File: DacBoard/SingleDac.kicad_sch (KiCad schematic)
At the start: 3 parts, among them U5 AD5725

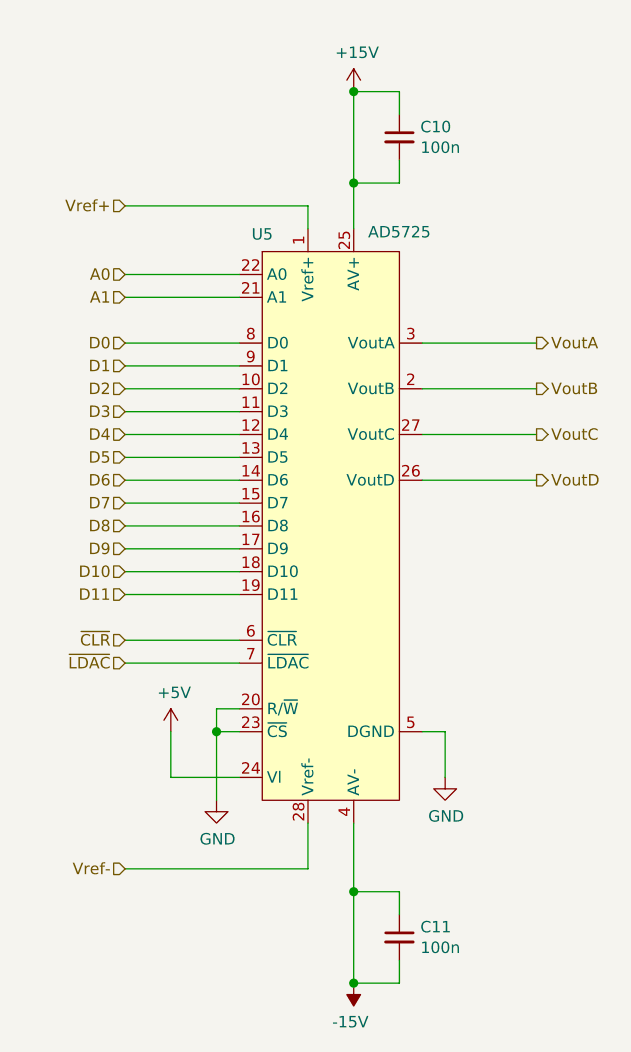
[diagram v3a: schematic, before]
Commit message: Schematic finalized (for now); Begin PCB
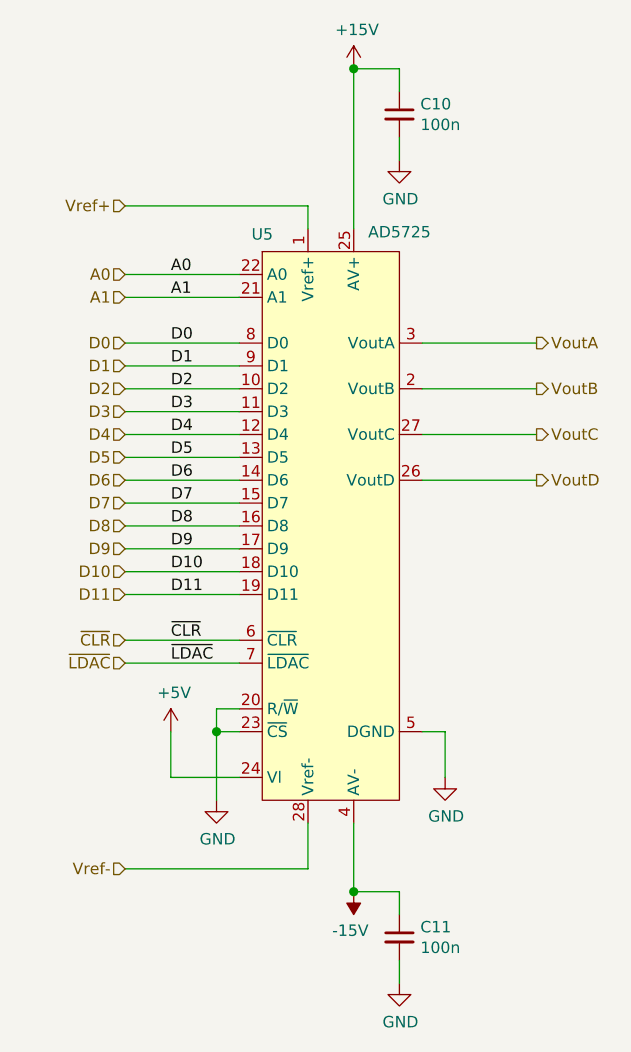
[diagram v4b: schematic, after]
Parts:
- C10, C11: footprint (none) -> Capacitor_SMD:C_0805_2012Metric_Pad1.18x1.45mm_HandSolder
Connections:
- net +15V: no longer C10.2
- net -15V: no longer C11.2
- net GND: now also C10.2, C11.2
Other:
- moved on the sheet: C10
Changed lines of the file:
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@@
   (paper "A4")
   (junction (at 167.64 104.14) (diameter 1.016) (color 0 0 0 0))
-  (junction (at 182.88 33.02) (diameter 1.016) (color 0 0 0 0))
-  (junction (at 182.88 43.18) (diameter 1.016) (color 0 0 0 0))
+  (junction (at 182.88 30.48) (diameter 1.016) (color 0 0 0 0))
   (junction (at 182.88 121.92) (diameter 1.016) (color 0 0 0 0))
-  (junction (at 182.88 132.08) (diameter 1.016) (color 0 0 0 0))
   (wire (pts (xy 157.48 45.72) (xy 177.8 45.72))
     (stroke (width 0) (type solid) (color 0 0 0 0))
@@
     (stroke (width 0) (type solid) (color 0 0 0 0))
   )
-  (wire (pts (xy 182.88 33.02) (xy 182.88 43.18))
-    (stroke (width 0) (type solid) (color 0 0 0 0))
-  )
-  (wire (pts (xy 182.88 33.02) (xy 187.96 33.02))
-    (stroke (width 0) (type solid) (color 0 0 0 0))
-  )
-  (wire (pts (xy 182.88 43.18) (xy 182.88 48.26))
-    (stroke (width 0) (type solid) (color 0 0 0 0))
-  )
-  (wire (pts (xy 182.88 43.18) (xy 187.96 43.18))
+  (wire (pts (xy 182.88 30.48) (xy 182.88 48.26))
+    (stroke (width 0) (type solid) (color 0 0 0 0))
+  )
+  (wire (pts (xy 182.88 30.48) (xy 187.96 30.48))
     (stroke (width 0) (type solid) (color 0 0 0 0))
   )
@@
     (stroke (width 0) (type solid) (color 0 0 0 0))
   )
-  (wire (pts (xy 182.88 132.08) (xy 182.88 121.92))
-    (stroke (width 0) (type solid) (color 0 0 0 0))
-  )
-  (wire (pts (xy 182.88 132.08) (xy 187.96 132.08))
-    (stroke (width 0) (type solid) (color 0 0 0 0))
-  )
-  (wire (pts (xy 187.96 33.02) (xy 187.96 35.56))
-    (stroke (width 0) (type solid) (color 0 0 0 0))
-  )
-  (wire (pts (xy 187.96 43.18) (xy 187.96 40.64))
+  (wire (pts (xy 187.96 30.48) (xy 187.96 33.02))
+    (stroke (width 0) (type solid) (color 0 0 0 0))
+  )
+  (wire (pts (xy 187.96 40.64) (xy 187.96 38.1))
     (stroke (width 0) (type solid) (color 0 0 0 0))
   )
@@
   (wire (pts (xy 193.04 104.14) (xy 193.04 109.22))
     (stroke (width 0) (type solid) (color 0 0 0 0))
+  )
+  (label "A0" (at 162.56 53.34 0)
+    (effects (font (size 1.27 1.27)) (justify left bottom))
+  )
+  (label "A1" (at 162.56 55.88 0)
+    (effects (font (size 1.27 1.27)) (justify left bottom))
+  )
+  (label "D0" (at 162.56 60.96 0)
+    (effects (font (size 1.27 1.27)) (justify left bottom))
+  )
+  (label "D1" (at 162.56 63.5 0)
+    (effects (font (size 1.27 1.27)) (justify left bottom))
+  )
+  (label "D2" (at 162.56 66.04 0)
+    (effects (font (size 1.27 1.27)) (justify left bottom))
+  )
+  (label "D3" (at 162.56 68.58 0)
+    (effects (font (size 1.27 1.27)) (justify left bottom))
+  )
+  (label "D4" (at 162.56 71.12 0)
+    (effects (font (size 1.27 1.27)) (justify left bottom))
+  )
+  (label "D5" (at 162.56 73.66 0)
+    (effects (font (size 1.27 1.27)) (justify left bottom))
+  )
+  (label "D6" (at 162.56 76.2 0)
+    (effects (font (size 1.27 1.27)) (justify left bottom))
+  )
+  (label "D7" (at 162.56 78.74 0)
+    (effects (font (size 1.27 1.27)) (justify left bottom))
+  )
+  (label "D8" (at 162.56 81.28 0)
+    (effects (font (size 1.27 1.27)) (justify left bottom))
+  )
+  (label "D9" (at 162.56 83.82 0)
+    (effects (font (size 1.27 1.27)) (justify left bottom))
+  )
+  (label "D10" (at 162.56 86.36 0)
+    (effects (font (size 1.27 1.27)) (justify left bottom))
+  )
+  (label "D11" (at 162.56 88.9 0)
+    (effects (font (size 1.27 1.27)) (justify left bottom))
+  )
+  (label "~CLR" (at 162.56 93.98 0)
+    (effects (font (size 1.27 1.27)) (justify left bottom))
+  )
+  (label "~LDAC" (at 162.56 96.52 0)
+    (effects (font (size 1.27 1.27)) (justify left bottom))
   )
   (hierarchical_label "Vref+" (shape input) (at 157.48 45.72 180)
@@
     (pin "1")
   )
-  (symbol (lib_id "power:+15V") (at 182.88 33.02 0)
-    (in_bom yes) (on_board yes)
-    (property "Reference" "#PWR0128" (id 0) (at 182.88 36.83 0)
-      (effects (font (size 1.27 1.27)) hide)
-    )
-    (property "Value" "+15V" (id 1) (at 183.2483 28.6956 0))
-    (property "Footprint" "" (id 2) (at 182.88 33.02 0)
-      (effects (font (size 1.27 1.27)) hide)
-    )
-    (property "Datasheet" "" (id 3) (at 182.88 33.02 0)
-      (effects (font (size 1.27 1.27)) hide)
-    )
-    (pin "1")
-  )
-  (symbol (lib_id "power:-15V") (at 182.88 132.08 180)
-    (in_bom yes) (on_board yes)
-    (property "Reference" "#PWR0131" (id 0) (at 182.88 134.62 0)
-      (effects (font (size 1.27 1.27)) hide)
-    )
-    (property "Value" "-15V" (id 1) (at 182.5117 136.4044 0))
-    (property "Footprint" "" (id 2) (at 182.88 132.08 0)
-      (effects (font (size 1.27 1.27)) hide)
-    )
-    (property "Datasheet" "" (id 3) (at 182.88 132.08 0)
+  (symbol (lib_id "power:+15V") (at 182.88 30.48 0)
+    (in_bom yes) (on_board yes)
+    (property "Reference" "#PWR0128" (id 0) (at 182.88 34.29 0)
+      (effects (font (size 1.27 1.27)) hide)
+    )
+    (property "Value" "+15V" (id 1) (at 183.2483 26.1556 0))
+    (property "Footprint" "" (id 2) (at 182.88 30.48 0)
+      (effects (font (size 1.27 1.27)) hide)
+    )
+    (property "Datasheet" "" (id 3) (at 182.88 30.48 0)
+      (effects (font (size 1.27 1.27)) hide)
+    )
+    (pin "1")
+  )
+  (symbol (lib_id "power:-15V") (at 182.88 121.92 180)
+    (in_bom yes) (on_board yes)
+    (property "Reference" "#PWR0131" (id 0) (at 182.88 124.46 0)
+      (effects (font (size 1.27 1.27)) hide)
+    )
+    (property "Value" "-15V" (id 1) (at 182.5117 126.2444 0))
+    (property "Footprint" "" (id 2) (at 182.88 121.92 0)
+      (effects (font (size 1.27 1.27)) hide)
+    )
+    (property "Datasheet" "" (id 3) (at 182.88 121.92 0)
       (effects (font (size 1.27 1.27)) hide)
     )
@@
     (pin "1")
   )
+  (symbol (lib_id "power:GND") (at 187.96 40.64 0)
+    (in_bom yes) (on_board yes)
+    (property "Reference" "#PWR012" (id 0) (at 187.96 46.99 0)
+      (effects (font (size 1.27 1.27)) hide)
+    )
+    (property "Value" "GND" (id 1) (at 188.0743 44.9644 0))
+    (property "Footprint" "" (id 2) (at 187.96 40.64 0)
+      (effects (font (size 1.27 1.27)) hide)
+    )
+    (property "Datasheet" "" (id 3) (at 187.96 40.64 0)
+      (effects (font (size 1.27 1.27)) hide)
+    )
+    (pin "1")
+  )
+  (symbol (lib_id "power:GND") (at 187.96 132.08 0)
+    (in_bom yes) (on_board yes)
+    (property "Reference" "#PWR013" (id 0) (at 187.96 138.43 0)
+      (effects (font (size 1.27 1.27)) hide)
+    )
+    (property "Value" "GND" (id 1) (at 188.0743 136.4044 0))
+    (property "Footprint" "" (id 2) (at 187.96 132.08 0)
+      (effects (font (size 1.27 1.27)) hide)
+    )
+    (property "Datasheet" "" (id 3) (at 187.96 132.08 0)
+      (effects (font (size 1.27 1.27)) hide)
+    )
+    (pin "1")
+  )
   (symbol (lib_id "power:GND") (at 193.04 109.22 0)
     (in_bom yes) (on_board yes)
@@
     (pin "1")
   )
-  (symbol (lib_id "Device:C_Small") (at 187.96 38.1 0)
-    (in_bom yes) (on_board yes)
-    (property "Reference" "C10" (id 0) (at 190.2842 36.9506 0)
+  (symbol (lib_id "Device:C_Small") (at 187.96 35.56 0)
+    (in_bom yes) (on_board yes)
+    (property "Reference" "C10" (id 0) (at 190.2842 34.4106 0)
       (effects (font (size 1.27 1.27)) (justify left))
     )
-    (property "Value" "100n" (id 1) (at 190.2968 39.243 0)
+    (property "Value" "100n" (id 1) (at 190.2968 36.703 0)
       (effects (font (size 1.27 1.27)) (justify left))
     )
-    (property "Footprint" "" (id 2) (at 187.96 38.1 0)
-      (effects (font (size 1.27 1.27)) hide)
-    )
-    (property "Datasheet" "~" (id 3) (at 187.96 38.1 0)
+    (property "Footprint" "Capacitor_SMD:C_0805_2012Metric_Pad1.18x1.45mm_HandSolder" (id 2) (at 187.96 35.56 0)
+      (effects (font (size 1.27 1.27)) hide)
+    )
+    (property "Datasheet" "~" (id 3) (at 187.96 35.56 0)
       (effects (font (size 1.27 1.27)) hide)
     )
@@
       (effects (font (size 1.27 1.27)) (justify left))
     )
-    (property "Footprint" "" (id 2) (at 187.96 127 0)
-      (effects (font (size 1.27 1.27)) hide)
-    )
+    (property "Footprint" "Capacitor_SMD:C_0805_2012Metric_Pad1.18x1.45mm_HandSolder" (id 2) (at 187.96 127 0)
+      (effects (font (size 1.27 1.27)) hide)
+    )

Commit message: Working on PCB layout
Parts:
- renumbered C10 to C8, C11 to C9, U5 to U4
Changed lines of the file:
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@@
   (symbol (lib_id "power:+5V") (at 162.56 104.14 0)
     (in_bom yes) (on_board yes)
-    (property "Reference" "#PWR0129" (id 0) (at 162.56 107.95 0)
+    (property "Reference" "#PWR03" (id 0) (at 162.56 107.95 0)
       (effects (font (size 1.27 1.27)) hide)
     )
@@
   (symbol (lib_id "power:+15V") (at 182.88 30.48 0)
     (in_bom yes) (on_board yes)
-    (property "Reference" "#PWR0128" (id 0) (at 182.88 34.29 0)
+    (property "Reference" "#PWR05" (id 0) (at 182.88 34.29 0)
       (effects (font (size 1.27 1.27)) hide)
     )
@@
   (symbol (lib_id "power:-15V") (at 182.88 121.92 180)
     (in_bom yes) (on_board yes)
-    (property "Reference" "#PWR0131" (id 0) (at 182.88 124.46 0)
+    (property "Reference" "#PWR06" (id 0) (at 182.88 124.46 0)
       (effects (font (size 1.27 1.27)) hide)
     )
@@
   (symbol (lib_id "power:GND") (at 167.64 111.76 0)
     (in_bom yes) (on_board yes)
-    (property "Reference" "#PWR0130" (id 0) (at 167.64 118.11 0)
+    (property "Reference" "#PWR04" (id 0) (at 167.64 118.11 0)
       (effects (font (size 1.27 1.27)) hide)
     )
@@
   (symbol (lib_id "power:GND") (at 187.96 40.64 0)
     (in_bom yes) (on_board yes)
-    (property "Reference" "#PWR012" (id 0) (at 187.96 46.99 0)
+    (property "Reference" "#PWR010" (id 0) (at 187.96 46.99 0)
       (effects (font (size 1.27 1.27)) hide)
     )
@@
   (symbol (lib_id "power:GND") (at 187.96 132.08 0)
     (in_bom yes) (on_board yes)
-    (property "Reference" "#PWR013" (id 0) (at 187.96 138.43 0)
+    (property "Reference" "#PWR011" (id 0) (at 187.96 138.43 0)
       (effects (font (size 1.27 1.27)) hide)
     )
@@
   (symbol (lib_id "power:GND") (at 193.04 109.22 0)
     (in_bom yes) (on_board yes)
-    (property "Reference" "#PWR08" (id 0) (at 193.04 115.57 0)
+    (property "Reference" "#PWR07" (id 0) (at 193.04 115.57 0)
       (effects (font (size 1.27 1.27)) hide)
     )
@@
   (symbol (lib_id "Device:C_Small") (at 187.96 35.56 0)
     (in_bom yes) (on_board yes)
-    (property "Reference" "C10" (id 0) (at 190.2842 34.4106 0)
+    (property "Reference" "C8" (id 0) (at 190.2842 34.4106 0)
       (effects (font (size 1.27 1.27)) (justify left))
     )
@@
   (symbol (lib_id "Device:C_Small") (at 187.96 127 0)
     (in_bom yes) (on_board yes)
-    (property "Reference" "C11" (id 0) (at 190.2842 125.8506 0)
+    (property "Reference" "C9" (id 0) (at 190.2842 125.8506 0)
       (effects (font (size 1.27 1.27)) (justify left))
     )
@@
   (symbol (lib_id "Unichip:AD5725") (at 180.34 50.8 0)
     (in_bom yes) (on_board yes)
-    (property "Reference" "U5" (id 0) (at 172.72 48.8758 0))
+    (property "Reference" "U4" (id 0) (at 172.72 48.8758 0))
     (property "Value" "AD5725" (id 1) (at 187.96 48.6345 0))
     (property "Footprint" "Package_SO:SSOP-28_5.3x10.2mm_P0.65mm" (id 2) (at 170.18 77.47 0)
@@
     )
     (pin "1")
-    (pin "2")
-    (pin "3")
-    (pin "4")
-    (pin "5")
-    (pin "6")
-    (pin "7")
-    (pin "8")
-    (pin "9")
     (pin "10")
     (pin "11")
@@
     (pin "18")
     (pin "19")
+    (pin "2")
     (pin "20")
     (pin "21")
@@
     (pin "27")
     (pin "28")
+    (pin "3")
+    (pin "4")
+    (pin "5")
+    (pin "6")
+    (pin "7")
+    (pin "8")
+    (pin "9")
   )
 )
